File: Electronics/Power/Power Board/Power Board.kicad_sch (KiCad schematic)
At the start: 4 parts

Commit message: Finished power board layout
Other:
- note removed: "SPDT Switch"
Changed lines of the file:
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@@
     (stroke (width 0) (type default))
-  )
-  (text "SPDT Switch" (at 91.44 106.68 0)
-    (effects (font (size 1.27 1.27)) (justify left bottom))
   )
   (symbol (lib_id "power:GND") (at 34.29 121.92 0) (unit 1)

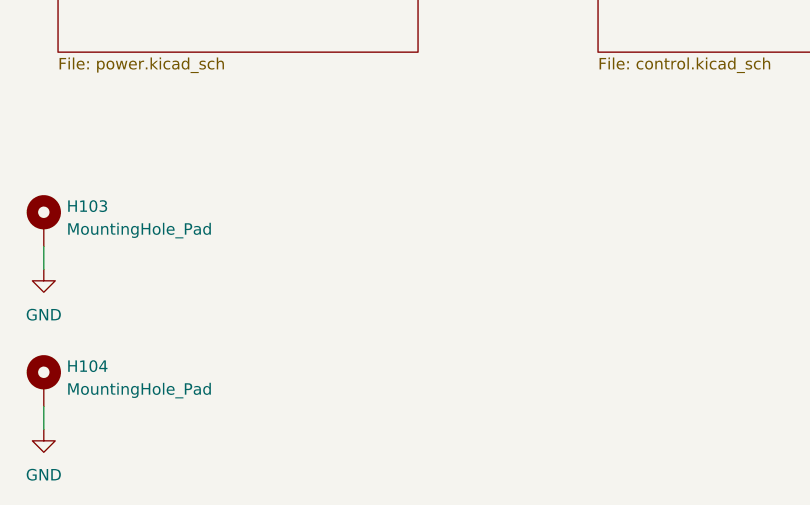
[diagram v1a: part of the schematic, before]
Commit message: Implemented power supply selector
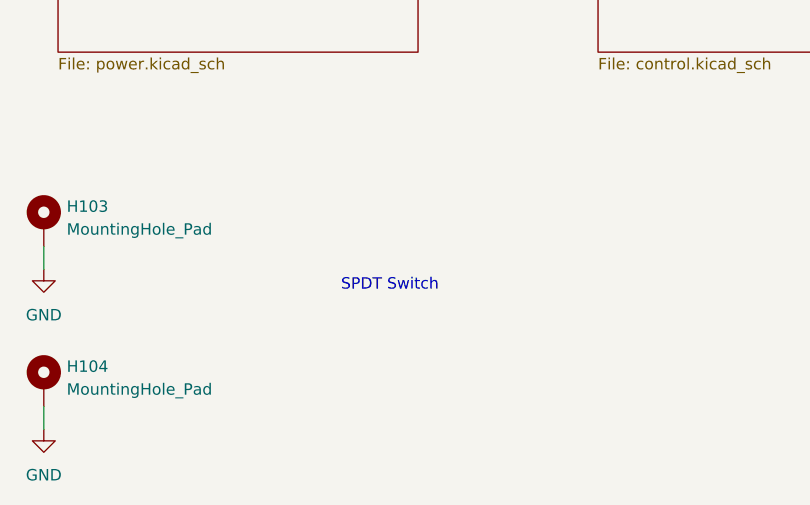
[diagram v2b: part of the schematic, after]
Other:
- note added: "SPDT Switch"
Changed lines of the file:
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@@
     (stroke (width 0) (type default))
+  )
+  (text "SPDT Switch" (at 91.44 106.68 0)
+    (effects (font (size 1.27 1.27)) (justify left bottom))
   )
   (symbol (lib_id "power:GND") (at 34.29 121.92 0) (unit 1)
